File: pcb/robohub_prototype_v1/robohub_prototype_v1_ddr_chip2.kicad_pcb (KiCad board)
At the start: 10 copper layers, 74 parts, among them J21 Barrel_Jack_Switch_Pin3Ring, J51 USB_A, J52 USB_A, J71 USB_A, U1 ATSAMA5D27C, U21 LM3880, U22 TPS564242DRL, U23 TPS564242DRL, U24 TPS564242DRL, U25 TPS564242DRL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

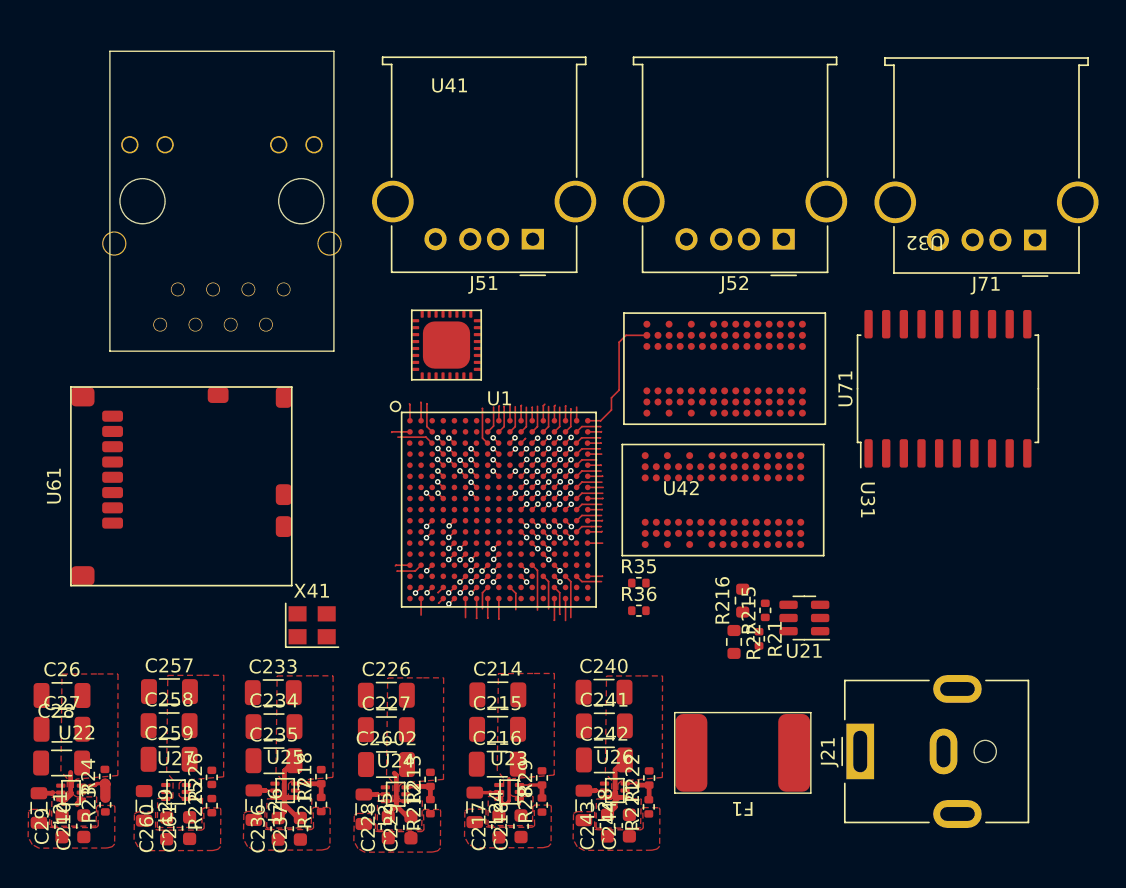
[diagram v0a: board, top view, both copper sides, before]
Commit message: Start routing ddr2
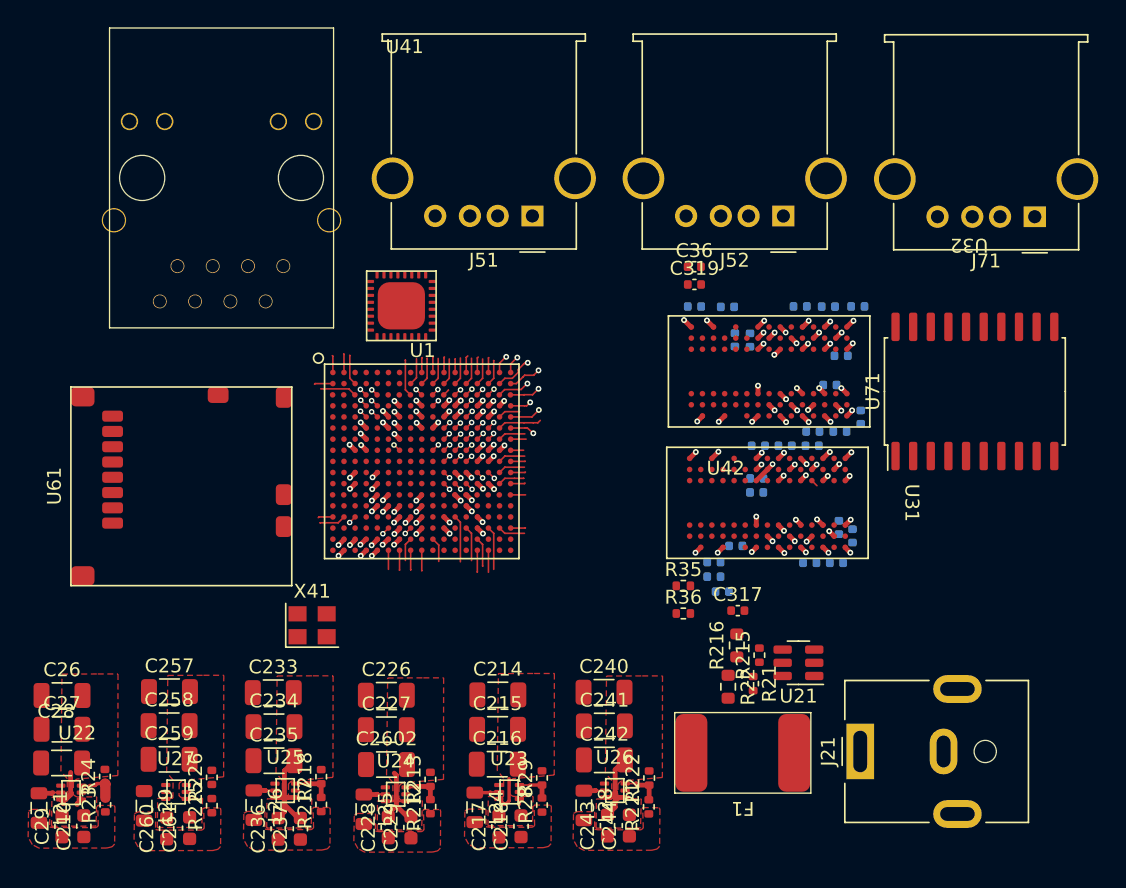
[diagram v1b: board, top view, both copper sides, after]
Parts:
- added C310: 100n, Capacitor_SMD:C_0402_1005Metric, B.Cu at (147.8, 87.9)
- added C311: 100n, Capacitor_SMD:C_0402_1005Metric, B.Cu at (151.9, 81.4)
- added C312: 100n, Capacitor_SMD:C_0402_1005Metric, B.Cu at (149.8, 87.9)
- added C313: 100n, Capacitor_SMD:C_0402_1005Metric, B.Cu at (151.1, 83.5)
- added C314: 1n, Capacitor_SMD:C_0402_1005Metric, B.Cu at (153.1, 77.9)
- added C315: 1n, Capacitor_SMD:C_0402_1005Metric, B.Cu at (150.9, 77.9)
- added C316: 1n, Capacitor_SMD:C_0402_1005Metric, B.Cu at (148.9, 77.9)
- added C317: 10u, Capacitor_SMD:C_0402_1005Metric, F.Cu at (144.4, 99.8)
- added C318: 1u, Capacitor_SMD:C_0402_1005Metric, B.Cu at (141.3, 77.9)
- added C319: 1u, Capacitor_SMD:C_0402_1005Metric, F.Cu at (141.3, 76.3)
- added C320: 100n, Capacitor_SMD:C_0402_1005Metric, B.Cu at (142.7, 96.3)
- added C321: 100n, Capacitor_SMD:C_0402_1005Metric, B.Cu at (151.5, 96.3)
- added C322: 100n, Capacitor_SMD:C_0402_1005Metric, B.Cu at (153.3, 85.8)
- added C323: 100n, Capacitor_SMD:C_0402_1005Metric, B.Cu at (151.8, 86.9)
- added C324: 100n, Capacitor_SMD:C_0402_1005Metric, B.Cu at (149.8, 86.9)
- added C325: 100n, Capacitor_SMD:C_0402_1005Metric, B.Cu at (151.7, 93.8)
- added C326: 1n, Capacitor_SMD:C_0402_1005Metric, B.Cu at (149.6, 96.3)
- added C327: 1n, Capacitor_SMD:C_0402_1005Metric, B.Cu at (152.7, 94.4)
- added C328: 1n, Capacitor_SMD:C_0402_1005Metric, B.Cu at (144.3, 95.1)
- added C33: 100n, Capacitor_SMD:C_0402_1005Metric, B.Cu at (145.3, 80.3)
- added C330: 100n, Capacitor_SMD:C_0402_1005Metric, B.Cu at (145.8, 90.2)
- added C331: 100nf, Capacitor_SMD:C_0402_1005Metric, B.Cu at (145.8, 91.3)
- added C34: 1n, Capacitor_SMD:C_0402_1005Metric, B.Cu at (144.2, 80.3)
- added C35: 10u, Capacitor_SMD:C_0402_1005Metric, B.Cu at (143.7, 77.9)
- added C36: 1u, Capacitor_SMD:C_0402_1005Metric, F.Cu at (141.3, 75.0)
- added C37: 1u, Capacitor_SMD:C_0402_1005Metric, B.Cu at (143.3, 98.4)
- added C38: 100n, Capacitor_SMD:C_0402_1005Metric, B.Cu at (142.7, 97.3)
- added C39: 100n, Capacitor_SMD:C_0402_1005Metric, B.Cu at (145.9, 87.9)
- moved U1 6.55 mm to (121.7, 89.0)
- moved U41 4.31 mm to (120.2, 77.8)
- moved R216 3.25 mm to (144.3, 102.3)
- moved U21 3.25 mm to (148.8, 103.5)
- moved R21 3.25 mm to (145.5, 105.0)
- moved R215 3.25 mm to (146.0, 103.0)
- moved R22 3.25 mm to (143.7, 105.2)
- moved U31 3.21 mm to (146.6, 92.0)
- moved U32 3.21 mm to (146.7, 82.5)
- moved R35 3.21 mm to (140.5, 98.0)
- moved R36 3.21 mm to (140.5, 100.0)
- moved U71 1.95 mm to (161.5, 84.0)
- moved J51 1.68 mm to (129.6, 71.4)
- moved J52 1.68 mm to (147.7, 71.4)
- moved U42 1.68 mm to (107.3, 68.6)
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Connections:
- U1 pad D16: Net-(C328-Pad1) -> DDR_VREF
- U1 pad H16: Net-(C328-Pad1) -> DDR_VREF
- U31 pad J2: /DDR2_3/DDR_VREF -> DDR_VREF
- U32 pad J2: /DDR2_3/DDR_VREF -> DDR_VREF
- U41 pad 2: /Ethernet_MAC_4/VDDA_1V2 -> VCC_1_2
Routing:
- net VCC_1_8_DDR: track 4.16 -> 24.0 mm, vias 7 -> 39
- net GND: track 44.4 -> 62.6 mm, vias 28 -> 60
- net /DDR2_3/DDR_A12: track 9.34 -> 1.38 mm, vias 0 -> 1
- net /DDR2_3/DDR_CS: track 0.65 -> 8.22 mm
- net /DDR2_3/DDR_A0: track 0.58 -> 6.69 mm
- net /DDR2_3/DDR_A13: track 0.57 -> 6.28 mm
- net /DDR2_3/DDR_CAS: track 0.60 -> 5.91 mm
- net /DDR2_3/DDR_A9: track 0.59 -> 5.67 mm
- net /DDR2_3/DDR_A7: track 0.61 -> 5.38 mm
- net /DDR2_3/DDR_A8: track 0.61 -> 5.01 mm
- net Net-(C328-Pad1): track 3.90 -> 0.00 mm
- net /DDR2_3/DDR_BA1: track 0.58 -> 4.29 mm
- net /DDR2_3/DDR_A10: track 0.59 -> 4.24 mm
- net /DDR2_3/DDR_RAS: track 0.61 -> 3.72 mm
- net /DDR2_3/DDR_BA0: track 0.59 -> 3.09 mm
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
